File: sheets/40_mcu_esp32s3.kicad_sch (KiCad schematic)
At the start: 0 parts

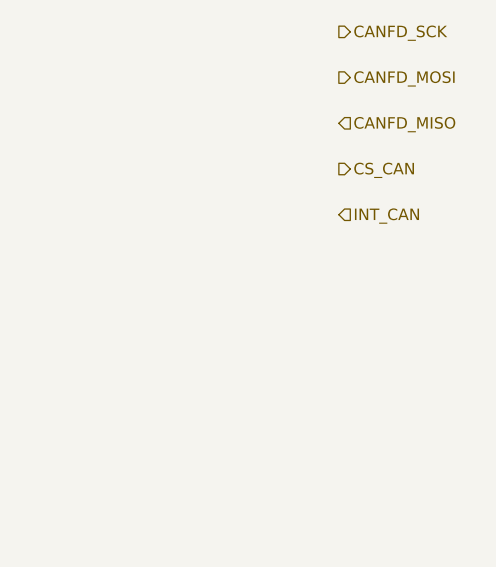
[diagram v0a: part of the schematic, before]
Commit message: Corrige la base del esquemático y añade reglas de proyecto
- Extrae el símbolo ADM3055E a lib/antmicro_adm3055ebriz.kicad_sym y lo
  registra en sym-lib-table con ${KIPRJMOD}.
- U1: huella Package_SO:SOIC-20W_7.5x12.8mm_P1.27mm (nota: verificar
  land pattern contra el datasheet).
- 10_power_input: power:GND -> GND_VEH; huellas y MPN de C1, C2 (0805
  X7R 100 V automotriz), C3 (EEE-HA2A470UP, 10x10) y F1 (1812, MPN
  pendiente).
- Nuevos pines jerárquicos CAN_SILENT (40_mcu -> 60_can, pull-down R1
  10k a GND_ISO) e IMU_INT2 (50_sensors -> 40_mcu).
- CLAUDE.md con reglas de librerías, campos, conexiones entre hojas,
  verificación por hoja y versión prototipo.
- Ignora output/ (reportes generados por kicad-mcp).

Co-Authored-By: Claude Opus 5.5 <noreply@anthropic.com>
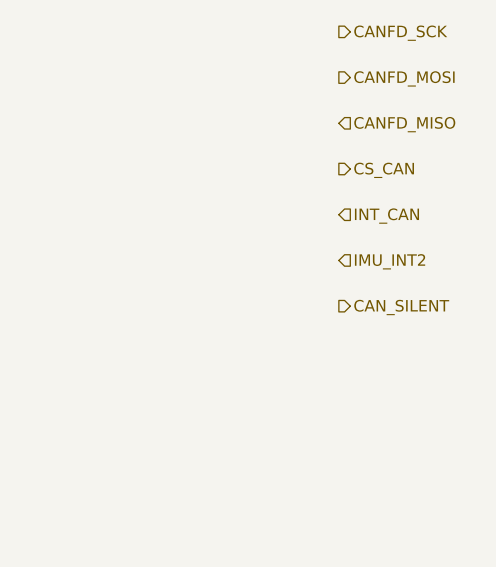
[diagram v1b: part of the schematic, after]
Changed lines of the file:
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@@
  (instances (project "INCLI-VA" (path "/7fd92c2b-4254-4d73-93ba-bfde861bede3/712b3cf0-3806-4b78-89c5-204f7bed5fb6" (reference "#PWR017") (unit 1)))))
 (embedded_fonts no)
+	(hierarchical_label "IMU_INT2"
+		(shape input)
+		(at 375.92 106.68 0)
+		(effects
+			(font
+				(size 1.27 1.27)
+			)
+			(justify left)
+		)
+	)
+	(hierarchical_label "CAN_SILENT"
+		(shape output)
+		(at 375.92 111.76 0)
+		(effects
+			(font
+				(size 1.27 1.27)
+			)
+			(justify left)
+		)
+	)
 )

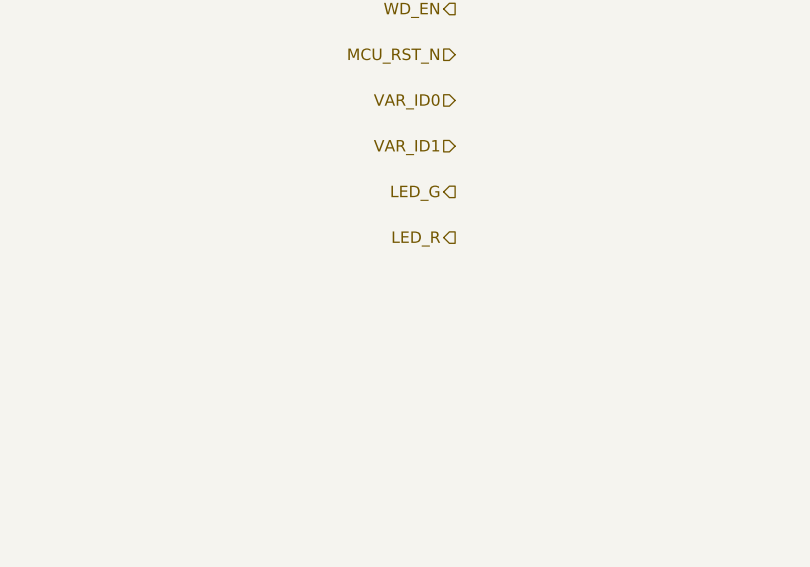
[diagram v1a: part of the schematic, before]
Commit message: 70_output: salida low-side con latch y señal PWR_FLT
- 70_output (DO1/DO2): MOSFET FDD7N25LZ (demo, 250 V) con TVS SMCJ188A
  en el drenador, latch de sobrecorriente a ~0.7 A (R 1 ohm + BC817/BC807,
  rearme con EN=0), apagado del gate por PWR_FLT_N o latch (BAT54A) y
  DIAG por divisor del drenador con zener 5V1. OUT pasa a pasivo.
- Jerarquía: VEH_PWR_FLT_N de 10_power_input a 70_output y 20_isolation;
  PWR_FLT de 20_isolation a 40_mcu (KW45 y ESP32-S3).
- 10_power_input: solo interfaz (VEH_DO1/2 pasivos, VEH_PWR_FLT_N);
  el circuito con LM74930 va en un commit aparte.
- CLAUDE.md: procedimiento para componentes fuera de las librerías.
- README: 70_output es low-side.

Co-Authored-By: Claude Opus 5.5 <noreply@anthropic.com>
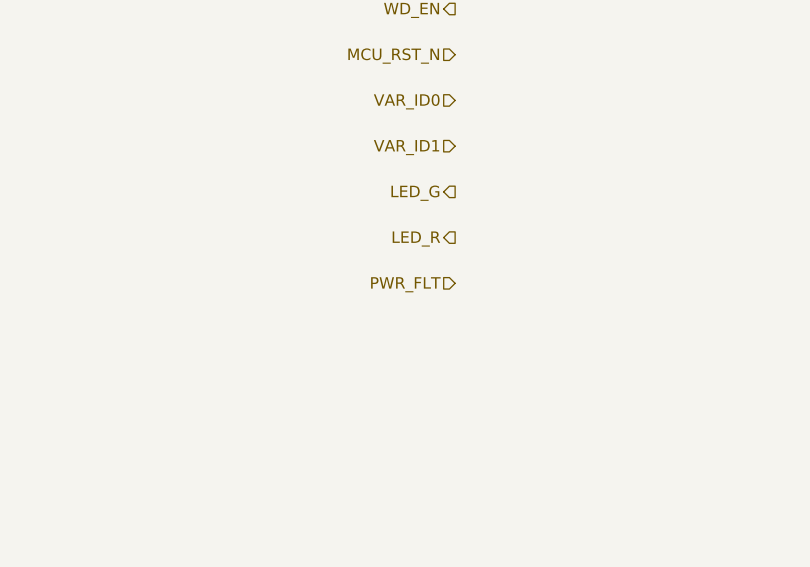
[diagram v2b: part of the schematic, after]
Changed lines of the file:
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@@
+		)
+	)
+	(hierarchical_label "PWR_FLT"
+		(shape input)
+		(at 238.76 96.52 180)
+		(effects
+			(font
+				(size 1.27 1.27)
+			)
+			(justify right)
 		)
 	)

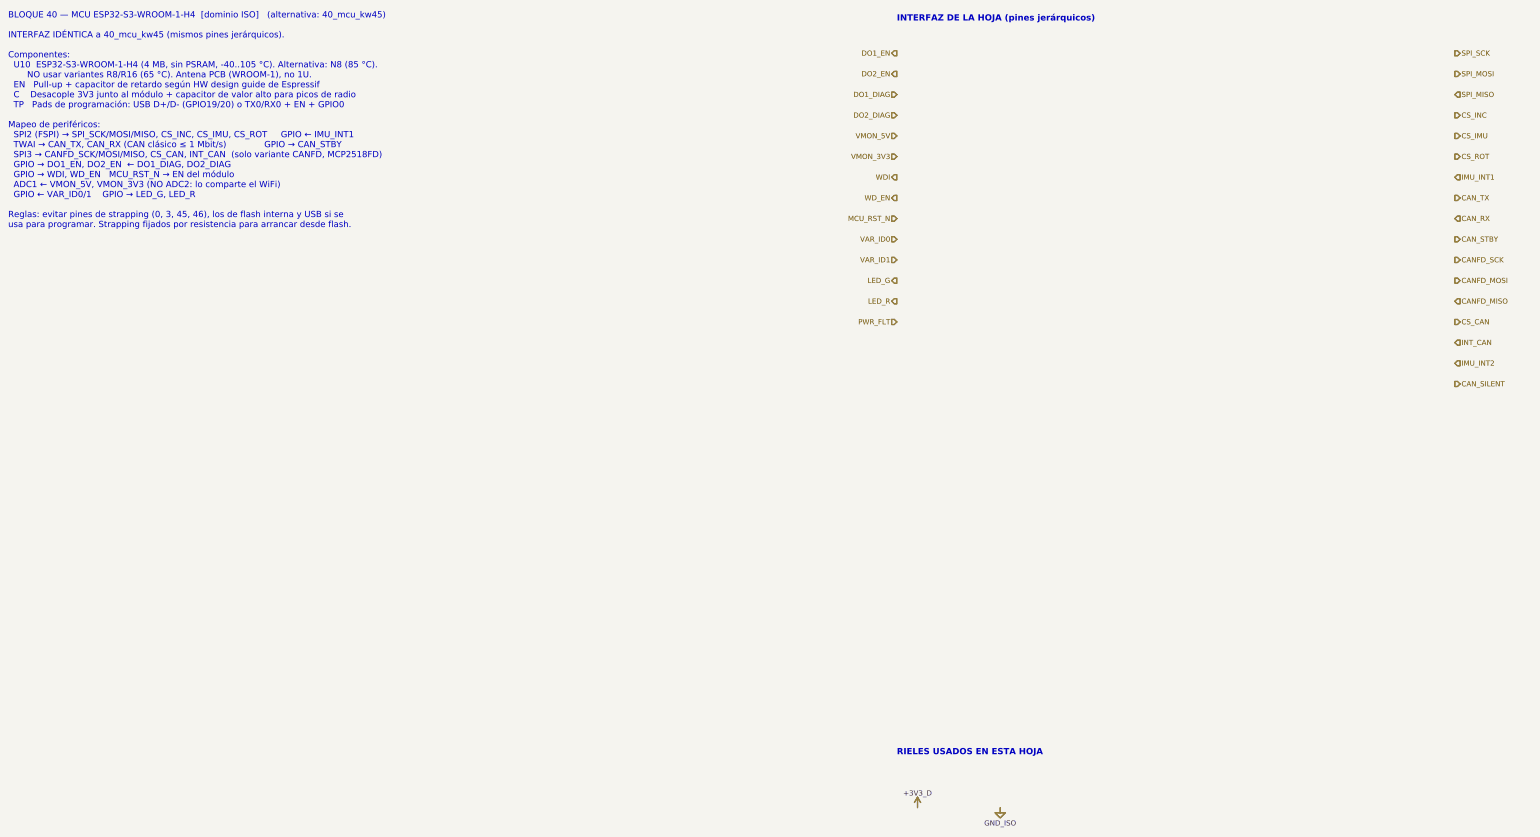
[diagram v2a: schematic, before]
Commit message: Alcance: solo ESP32-S3, CAN clásico por TWAI, sin MCP2518FD
- Raíz: el bloque 40_mcu apunta a 40_mcu_esp32s3. 40_mcu_kw45 queda en
  el repo solo como referencia, fuera de la jerarquía.
- CAN: se eliminan el MCP2518FD, el cristal y los pines CANFD_SCK/MOSI/
  MISO, CS_CAN e INT_CAN en 60_can, 40_mcu_esp32s3 y la raíz (etiquetas,
  cables y pines de hoja). TWAI nativo (J1939) directo al ADM3055E.
  Se quita la variante CANFD.
- 20_isolation (nota): PS1 >= 5 W y entrada 9-72 V (corte OV 38.4 V);
  U2 = TPS7A1650-Q1 para +5V_VEH.
- 40_mcu_esp32s3 (nota): desacople 22 uF + 100 nF según Espressif y
  límite de 47 uF en +3V3_D por el TPS62A02-Q1; solo BLE en operación.
- README: tabla corregida (LM74930-Q1 en 10_power_input, 20, 30, 40, 60),
  sección MCU y "Requisitos para el firmware" (rearme del latch >= 100 ms,
  arranque limpio tras brownout, NimBLE con WiFi desactivado).
- CLAUDE.md: sección "Alcance" (ESP32-S3 único, dimensionar con WiFi).

ERC: 180 -> 160 violaciones; sin errores nuevos. Las restantes son de
hojas sin terminar (20, 30, 60) y etiquetas de la raíz sin destino.

Co-Authored-By: Claude Opus 5.5 <noreply@anthropic.com>
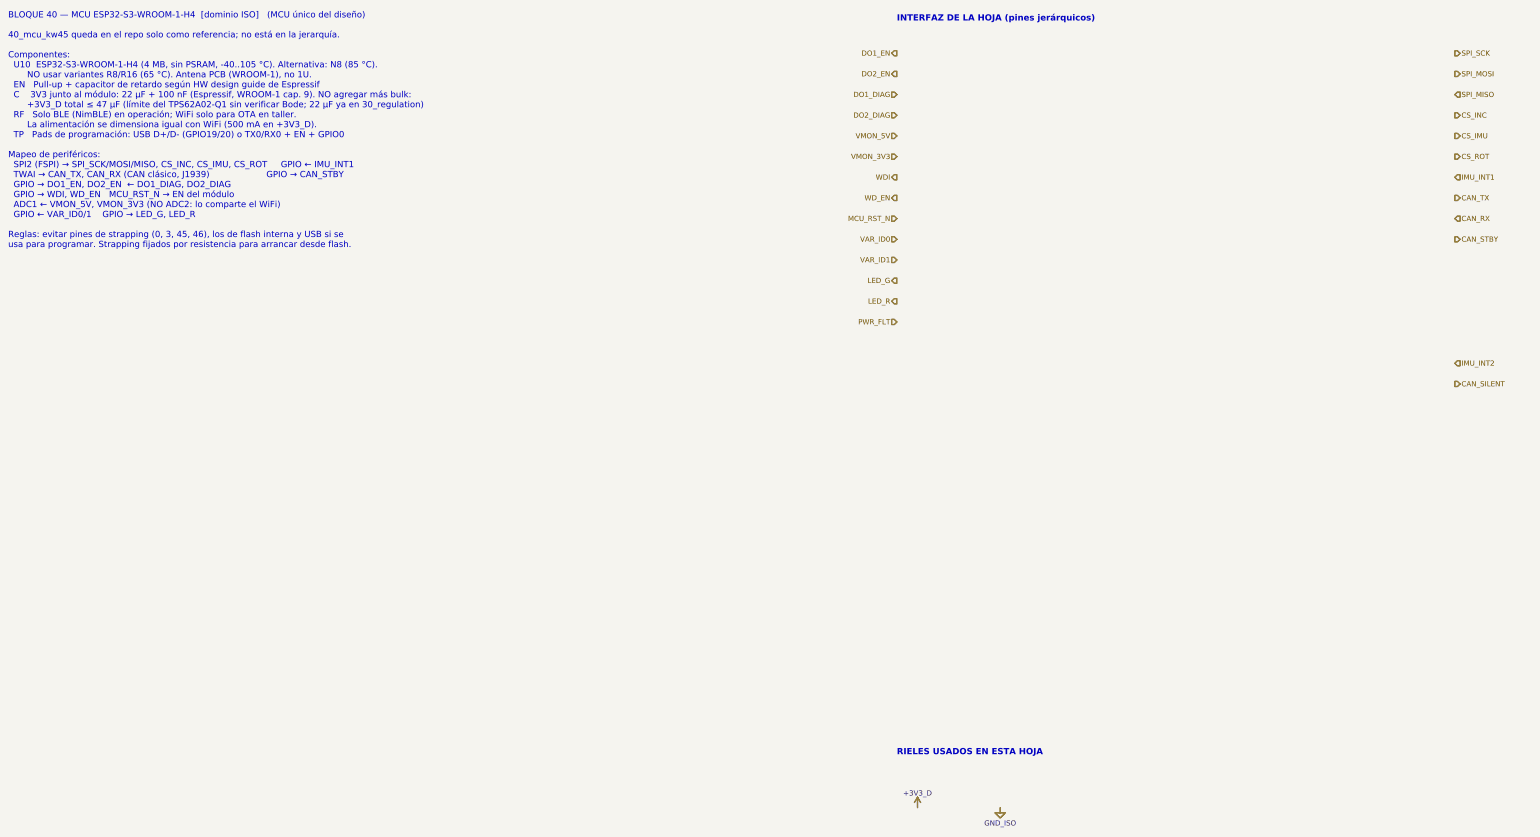
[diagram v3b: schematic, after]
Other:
- note added: "BLOQUE 40 — MCU ESP32-S3-WROOM-1-H4 [dominio ISO] (MCU único del diseño) 40_mcu_kw45 queda en el repo solo como referencia; no está en la jerarquía. Componentes: U10 ESP32-S3-WROOM-1-H4 (4 MB, sin PSRAM, -40..105 °C). Alternativa: N8 (85 °C). NO usar variantes R8/R16 (65 °C). Antena PCB (WROOM-1), no 1U. EN Pull-up + capacitor de retardo según HW design guide de Espressif C 3V3 junto al módulo: 2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"
- note removed: "BLOQUE 40 — MCU ESP32-S3-WROOM-1-H4 [dominio ISO] (alternativa: 40_mcu_kw45) INTERFAZ IDÉNTICA a 40_mcu_kw45 (mismos pines jerárquicos). Componentes: U10 ESP32-S3-WROOM-1-H4 (4 MB, sin PSRAM, -40..105 °C). Alternativa: N8 (85 °C). NO usar variantes R8/R16 (65 °C). Antena PCB (WROOM-1), no 1U. EN Pull-up + capacitor de retardo según HW design guide de Espressif C Desacople 3V3 junto al módulo + ca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"
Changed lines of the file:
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@@
 (paper "A3")
 (title_block (title "MCU ESP32-S3-WROOM-1-H4") (date "2026-10-24") (rev "A") (company "") (comment 1 "Hoja 40_mcu_esp32s3") (comment 2 "Inclinómetro de chasis CAN/BLE — INCLI-VA"))
-(text "BLOQUE 40 — MCU ESP32-S3-WROOM-1-H4  [dominio ISO]   (alternativa: 40_mcu_kw45)\n\nINTERFAZ IDÉNTICA a 40_mcu_kw45 (mismos pines jerárquicos).\n\nComponentes:\n  U10  ESP32-S3-WROOM-1-H4 (4 MB, sin PSRAM, -40..105 °C). Alternativa: N8 (85 °C).\n       NO usar variantes R8/R16 (65 °C). Antena PCB (WROOM-1), no 1U.\n  EN   Pull-up + capacitor de retardo según HW design guide de Espressif\n  C    Desacople 3V3 junto al módulo + capacitor de valor alto para picos de radio\n  TP   Pads de programación: USB D+/D- (GPIO19/20) o TX0/RX0 + EN + GPIO0\n\nMapeo de periféricos:\n  SPI2 (FSPI) → SPI_SCK/MOSI/MISO, CS_INC, CS_IMU, CS_ROT     GPIO ← IMU_INT1\n  TWAI → CAN_TX, CAN_RX (CAN clásico ≤ 1 Mbit/s)              GPIO → CAN_STBY\n  SPI3 → CANFD_SCK/MOSI/MISO, CS_CAN, INT_CAN  (solo variante CANFD, MCP2518FD)\n  GPIO → DO1_EN, DO2_EN  ← DO1_DIAG, DO2_DIAG\n  GPIO → WDI, WD_EN   MCU_RST_N → EN del módulo\n  ADC1 ← VMON_5V, VMON_3V3 (NO ADC2: lo comparte el WiFi)\n  GPIO ← VAR_ID0/1    GPIO → LED_G, LED_R\n\nReglas: evitar pines de strapping (0, 3, 45, 46), los de flash interna y USB si se\nusa para programar. Strapping fijados por resistencia para arrancar desde flash." (exclude_from_sim no) (at 20.32 20.32 0) (effects (font (size 1.524 1.524)) (justify left top)))
+(text "BLOQUE 40 — MCU ESP32-S3-WROOM-1-H4  [dominio ISO]   (MCU único del diseño)\n\n40_mcu_kw45 queda en el repo solo como referencia; no está en la jerarquía.\n\nComponentes:\n  U10  ESP32-S3-WROOM-1-H4 (4 MB, sin PSRAM, -40..105 °C). Alternativa: N8 (85 °C).\n       NO usar variantes R8/R16 (65 °C). Antena PCB (WROOM-1), no 1U.\n  EN   Pull-up + capacitor de retardo según HW design guide de Espressif\n  C    3V3 junto al módulo: 22 µF + 100 nF (Espressif, WROOM-1 cap. 9). NO agregar más bulk:\n       +3V3_D total ≤ 47 µF (límite del TPS62A02-Q1 sin verificar Bode; 22 µF ya en 30_regulation)\n  RF   Solo BLE (NimBLE) en operación; WiFi solo para OTA en taller.\n       La alimentación se dimensiona igual con WiFi (500 mA en +3V3_D).\n  TP   Pads de programación: USB D+/D- (GPIO19/20) o TX0/RX0 + EN + GPIO0\n\nMapeo de periféricos:\n  SPI2 (FSPI) → SPI_SCK/MOSI/MISO, CS_INC, CS_IMU, CS_ROT     GPIO ← IMU_INT1\n  TWAI → CAN_TX, CAN_RX (CAN clásico, J1939)                     GPIO → CAN_STBY\n  GPIO → DO1_EN, DO2_EN  ← DO1_DIAG, DO2_DIAG\n  GPIO → WDI, WD_EN   MCU_RST_N → EN del módulo\n  ADC1 ← VMON_5V, VMON_3V3 (NO ADC2: lo comparte el WiFi)\n  GPIO ← VAR_ID0/1    GPIO → LED_G, LED_R\n\nReglas: evitar pines de strapping (0, 3, 45, 46), los de flash interna y USB si se\nusa para programar. Strapping fijados por resistencia para arrancar desde flash." (exclude_from_sim no) (at 20.32 20.32 0) (effects (font (size 1.524 1.524)) (justify left top)))
 (text "INTERFAZ DE LA HOJA (pines jerárquicos)" (exclude_from_sim no) (at 238.76 22.86 0) (effects (font (size 1.524 1.524) (bold yes)) (justify left bottom)))
 (hierarchical_label "DO1_EN" (shape output) (at 238.76 30.48 180) (effects (font (size 1.27 1.27)) (justify right)))
@@
 (hierarchical_label "CAN_RX" (shape input) (at 375.92 71.12 0) (effects (font (size 1.27 1.27)) (justify left)))
 (hierarchical_label "CAN_STBY" (shape output) (at 375.92 76.20 0) (effects (font (size 1.27 1.27)) (justify left)))
-(hierarchical_label "CANFD_SCK" (shape output) (at 375.92 81.28 0) (effects (font (size 1.27 1.27)) (justify left)))
-(hierarchical_label "CANFD_MOSI" (shape output) (at 375.92 86.36 0) (effects (font (size 1.27 1.27)) (justify left)))
-(hierarchical_label "CANFD_MISO" (shape input) (at 375.92 91.44 0) (effects (font (size 1.27 1.27)) (justify left)))
-(hierarchical_label "CS_CAN" (shape output) (at 375.92 96.52 0) (effects (font (size 1.27 1.27)) (justify left)))
-(hierarchical_label "INT_CAN" (shape input) (at 375.92 101.60 0) (effects (font (size 1.27 1.27)) (justify left)))
 (text "RIELES USADOS EN ESTA HOJA" (exclude_from_sim no) (at 238.76 203.20 0) (effects (font (size 1.524 1.524) (bold yes)) (justify left bottom)))
 (symbol (lib_id "INCLI-VA:+3V3_D") (at 243.84 215.90 0) (unit 1) (exclude_from_sim no) (in_bom no) (on_board yes) (dnp no)

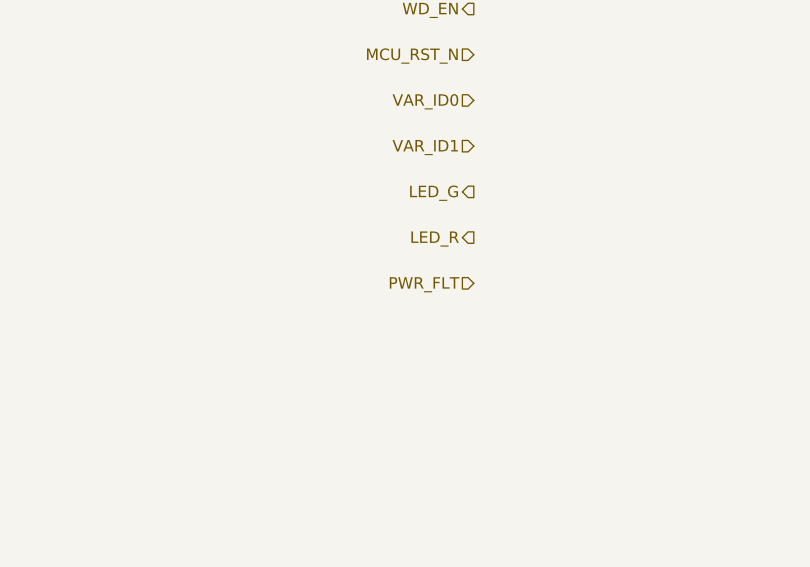
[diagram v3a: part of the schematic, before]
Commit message: 20_isolation: PS201 EC4AW8-48S05, LDO +5V_VEH, ISO7763-Q1; PWR_FLT_N; L301 HandSolder
- Hoja 20 completa: PS201 Cincon EC4AW8-48S05 (sin Remote On/Off) con
  C201/C202/C203; U201 TPS7A1650-Q1 (+VPROT -> +5V_VEH; DELAY, PG y FB/NC
  abiertos según TI SBVS188E tabla 5-1); U202 ISO7763FQDWRQ1 con pull-downs
  R201-R204; notas de distancias de la barrera 1.
- Símbolo INCLI-VA:EC4AW8-48S05 creado desde la tabla de pines del datasheet
  Cincon V10 (excepción autorizada); huella oficial TRACO THD 15WIN verificada.
- Renombre PWR_FLT -> PWR_FLT_N en la raíz, 20 y 40_mcu.
- Huella INCLI-VA:L_Coilcraft_XAL4020_HandSolder (Coilcraft Doc 806-4,
  rev. 02/25/26) asignada a L301.
- Datasheets de EC4AW8 y XAL4020 en docs/datasheets.
- ERC: 0 en 20 y 30 (129 en el proyecto); sch_visual_qa PASS en 20.

Co-Authored-By: Claude Opus 5.5 <noreply@anthropic.com>
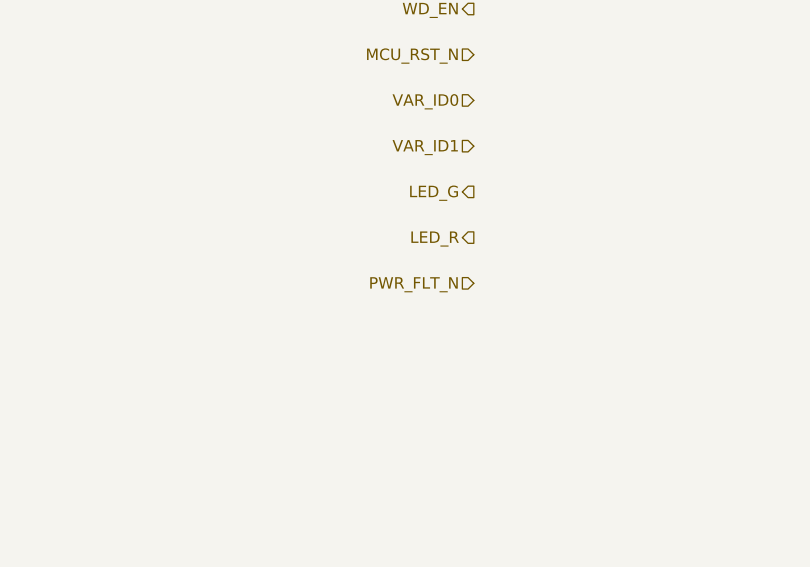
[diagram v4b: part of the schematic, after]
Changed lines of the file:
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@@
 		)
 	)
-	(hierarchical_label "PWR_FLT"
+	(hierarchical_label "PWR_FLT_N"
 		(shape input)
 		(at 238.76 96.52 180)
